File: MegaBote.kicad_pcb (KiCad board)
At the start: 4 copper layers, 45 x 45 mm, 40 parts, among them J1 USB_B_Mini, J2 J1962, J3 Micro_SD_Card, J4 Conn_02x05_Odd_Even, U1 SN65HVD230, U2 AMS1117-3.3, U3 USBLC6-2SC6, U4 STM32F105RBTx

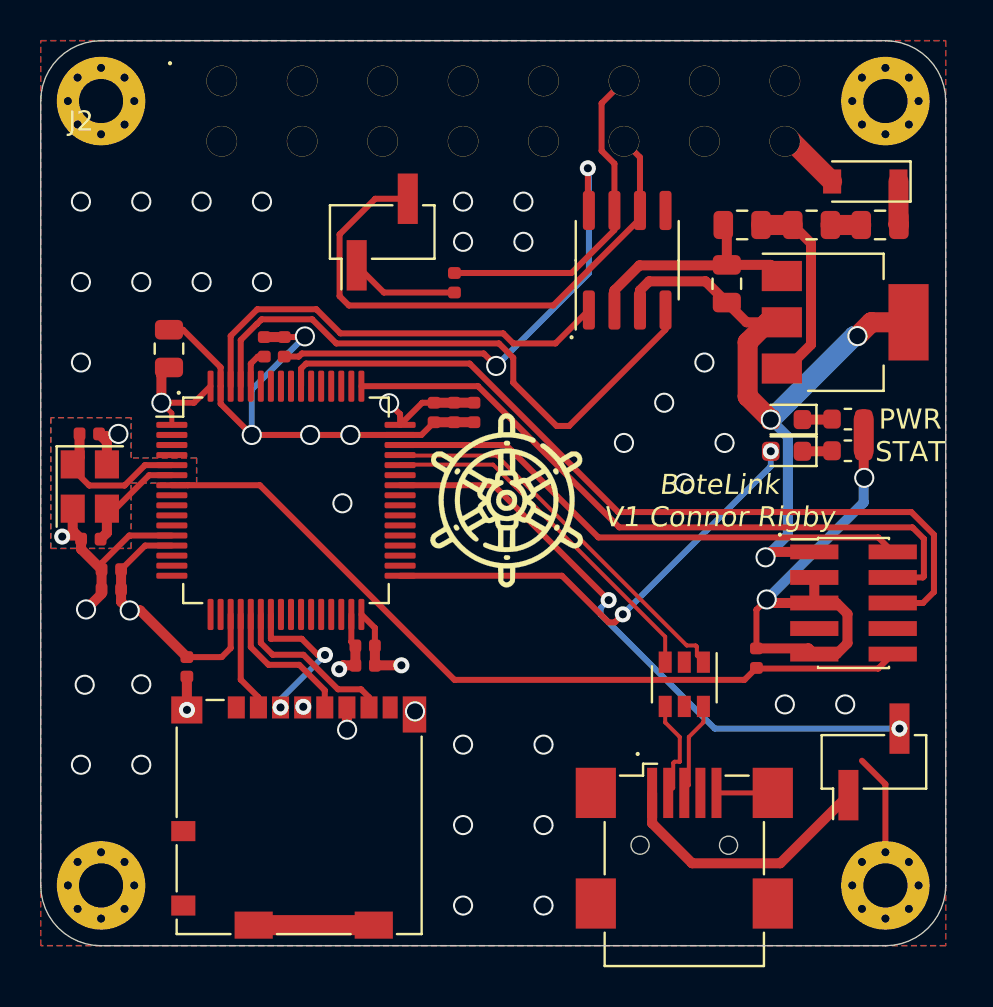
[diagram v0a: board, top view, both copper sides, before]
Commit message: Fix OBD2 footprint
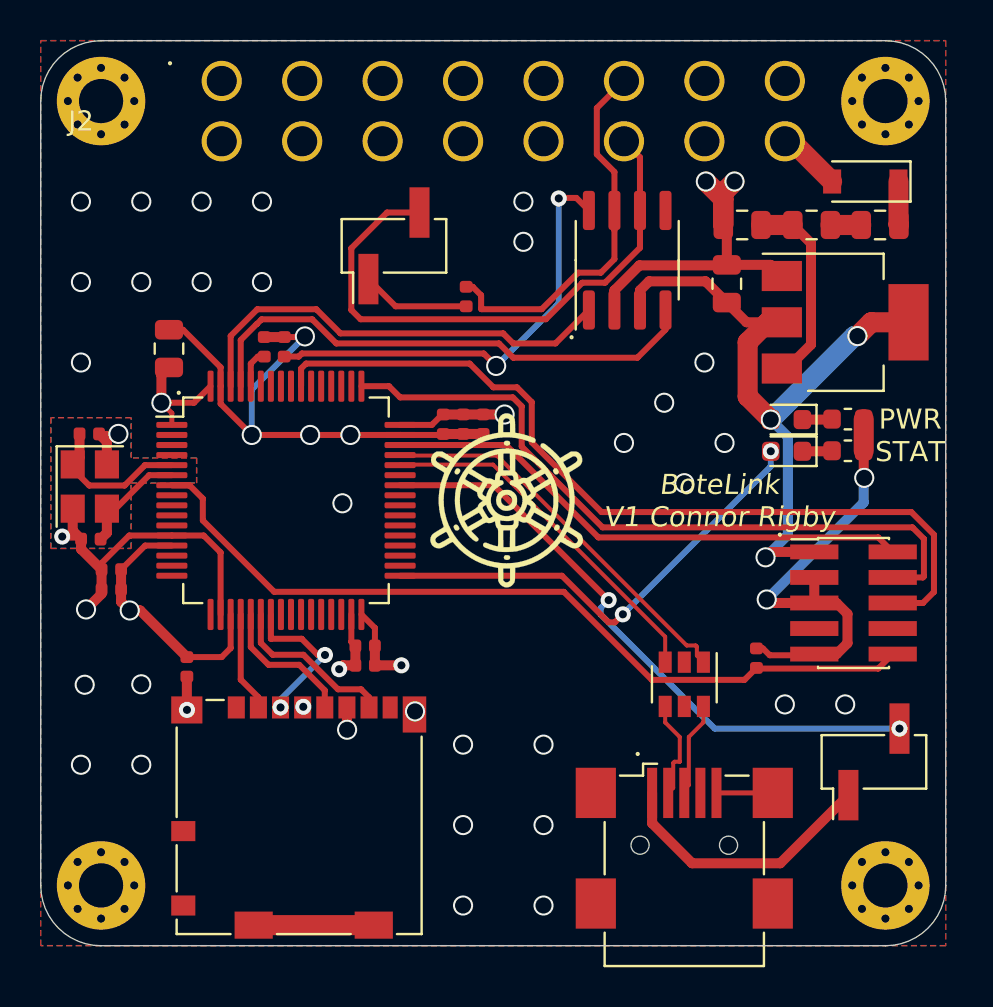
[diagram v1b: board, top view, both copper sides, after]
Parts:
- moved JP2 0.90 mm to (187.6, 100.2)
- moved R2 0.90 mm to (191.2, 102.7)
- moved C7 0.74 mm to (190.0, 109.1)
- moved C2 0.74 mm to (191.0, 109.1)
- moved C6 0.74 mm to (192.0, 109.1)
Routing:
- net CAN1_RX: track 29.7 -> 26.2 mm
- net Net-(R1-Pad1): track 24.7 -> 22.3 mm
- net GND: track 94.3 -> 96.6 mm
- net CANH: track 17.0 -> 19.0 mm
- net NRST: track 40.4 -> 41.8 mm
- net SWCLK: track 34.6 -> 35.7 mm
- net SWO: track 41.1 -> 42.3 mm
- net CANL: track 28.3 -> 29.2 mm

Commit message: Address a few nits in the pcb
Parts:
- moved C11 7.37 mm to (212.9, 121.9), turned to 0 degrees
- moved C4 4.85 mm to (172.2, 107.7), turned to 0 degrees
- moved C5 4.73 mm to (173.5, 118.3), turned to 180 degrees
- moved G*** 2.41 mm to (195.6, 112.9)
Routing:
- net GND: track 96.6 -> 75.2 mm, vias 44 -> 34
- net +3V3: track 64.6 -> 83.5 mm, vias 8 -> 6
- net Net-(D3-Pad2): track 23.4 -> 24.3 mm
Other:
- board text added: "CAN"
- board text added: "VBUS"
